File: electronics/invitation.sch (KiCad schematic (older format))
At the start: 40 parts, among them P1 USB Micro B, P10 Up Arrow, P11 Down Arrow, P2 Home btn, P3 Bottom Connections 1, P4 Left Arrow, P5 Right Arrow, P8 CONN_01X01, P9 CONN_01X02, U1 ATMEGA32U4-A, Y1 16 FA-238 Mhz

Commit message: Hero text fix + vr fix
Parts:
- P10: footprint newAssets:upArrow -> newAssets:upArrowSS
- P11: footprint newAssets:downArrow -> newAssets:downArrowSS
- P4: footprint newAssets:leftArrow -> newAssets:leftArrowSS
- P5: footprint newAssets:rightArrow -> newAssets:rightArrowSS
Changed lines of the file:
@@
 F 0 "P4" H 10050 2950 50  0000 C CNN
 F 1 "Left Arrow" H 10350 2850 50  0000 C CNN
-F 2 "newAssets:leftArrow" H 10050 2850 50  0001 C CNN
+F 2 "newAssets:leftArrowSS" H 10050 2850 50  0001 C CNN
 F 3 "" H 10050 2850 50  0000 C CNN
 	1    10050 2850
@@
 F 0 "P5" H 10100 3950 50  0000 C CNN
 F 1 "Right Arrow" H 10400 3850 50  0000 C CNN
-F 2 "newAssets:rightArrow" H 10100 3850 50  0001 C CNN
+F 2 "newAssets:rightArrowSS" H 10100 3850 50  0001 C CNN
 F 3 "" H 10100 3850 50  0000 C CNN
 	1    10100 3850
@@
 F 0 "P10" H 10000 5150 50  0000 C CNN
 F 1 "Up Arrow" H 10250 5050 50  0000 C CNN
-F 2 "newAssets:upArrow" H 10000 5050 50  0001 C CNN
+F 2 "newAssets:upArrowSS" H 10000 5050 50  0001 C CNN
 F 3 "" H 10000 5050 50  0000 C CNN
 	1    10000 5050
@@
 F 0 "P11" H 10100 6300 50  0000 C CNN
 F 1 "Down Arrow" H 10400 6200 50  0000 C CNN
-F 2 "newAssets:downArrow" H 10100 6200 50  0001 C CNN
+F 2 "newAssets:downArrowSS" H 10100 6200 50  0001 C CNN
 F 3 "" H 10100 6200 50  0000 C CNN
 	1    10100 6200

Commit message: pub in progress
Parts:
- P2: footprint newAssets:JMLogoFinal -> newAssets:JMLogoFinalSS
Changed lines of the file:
@@
 F 0 "P2" H 10100 1950 50  0000 C CNN
 F 1 "Home btn" H 10400 1850 50  0000 C CNN
-F 2 "newAssets:JMLogoFinal" H 10100 1850 50  0001 C CNN
+F 2 "newAssets:JMLogoFinalSS" H 10100 1850 50  0001 C CNN
 F 3 "" H 10100 1850 50  0000 C CNN
 	1    10100 1850

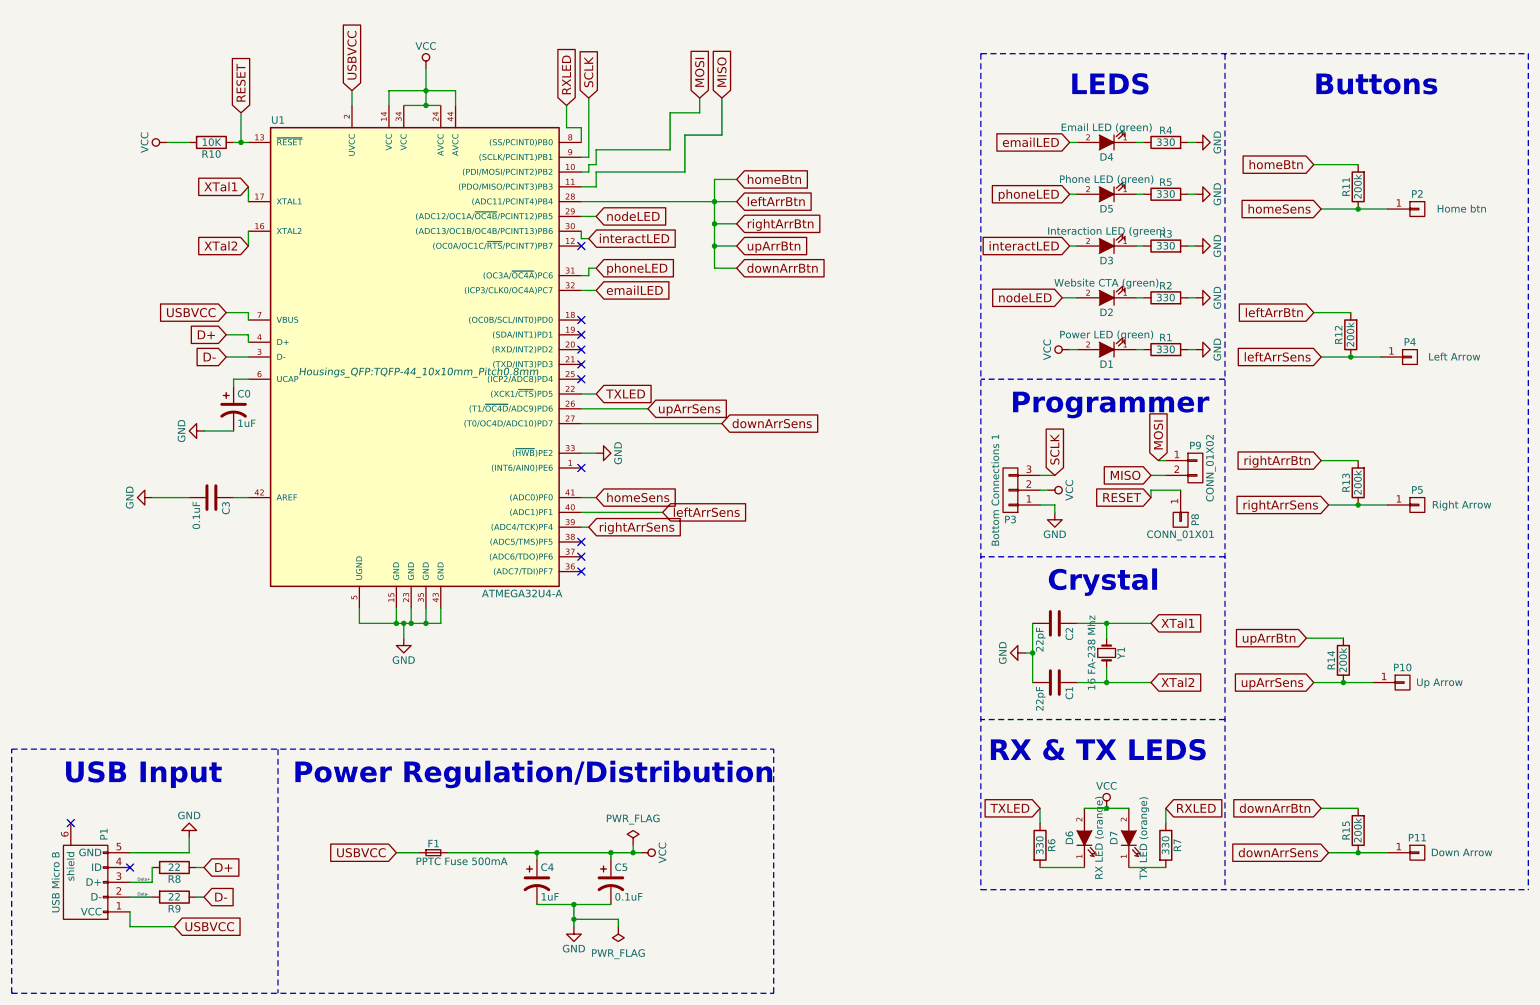
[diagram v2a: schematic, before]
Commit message: Business card finished.
To do:
- Implement keyboard functionality to website
- Test Arduino code + electronics
- Get electronics card purchased
- Implement instructions for VR page on desktop
- Final check of website copy prior to getting biz cards reprinted
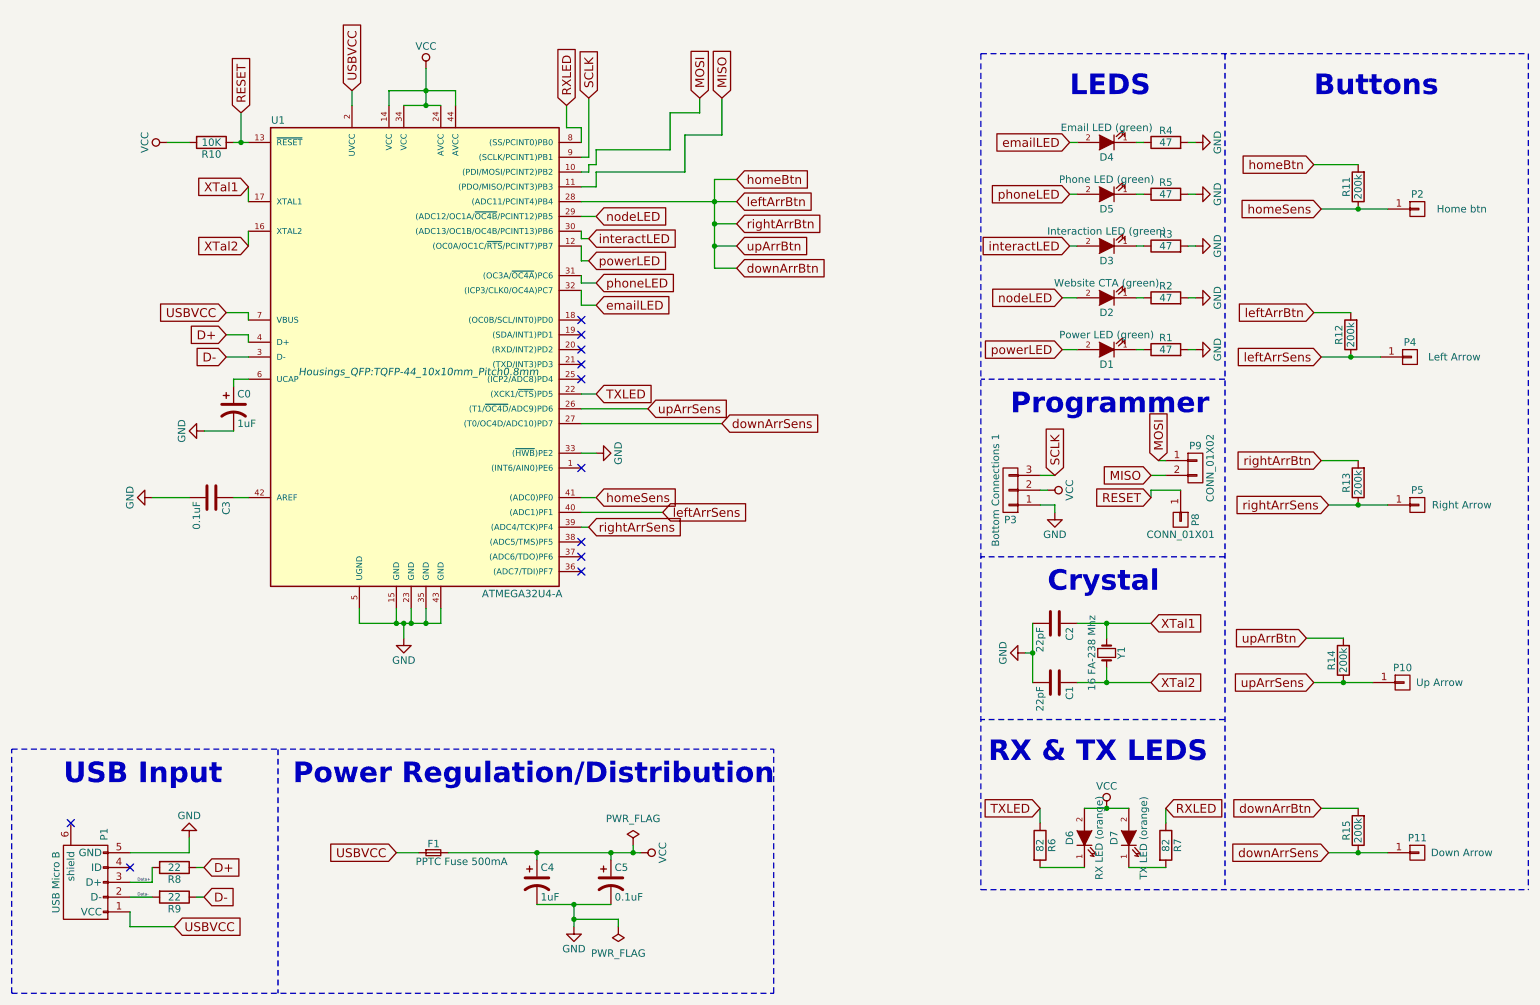
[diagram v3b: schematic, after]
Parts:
- R1, R2, R3, R4, R5: value 330 -> 47
- R6, R7: value 330 -> 82
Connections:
- net VCC: no longer D1.2 (A)
- net powerLED: now reaches U1.12 ((OC0A/OC1C/~RTS~/PCINT7)PB7)
- net powerLED: now also D1.2 (A)
- no-connect marks 12 -> 11
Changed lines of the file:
@@
 Sheet 1 1
 Title "Portfolio Business Card"
-Date "January 2017"
+Date "November 2018"
 Rev "1"
 Comp "James Miller"
@@
 P 7550 6150
 F 0 "R6" V 7630 6150 50  0000 C CNN
-F 1 "330" V 7550 6150 50  0000 C CNN
+F 1 "82" V 7550 6150 50  0000 C CNN
 F 2 "Resistors_SMD:R_0805" V 7480 6150 50  0001 C CNN
 F 3 "" H 7550 6150 50  0000 C CNN
@@
 P 8400 6150
 F 0 "R7" V 8480 6150 50  0000 C CNN
-F 1 "330" V 8400 6150 50  0000 C CNN
+F 1 "82" V 8400 6150 50  0000 C CNN
 F 2 "Resistors_SMD:R_0805" V 8330 6150 50  0001 C CNN
 F 3 "" H 8400 6150 50  0000 C CNN
@@
 	1    0    0    -1
 $EndComp
-NoConn ~ 4450 2100
 $Comp
 L power:GND #PWR06
@@
 $EndComp
 $Comp
-L power:VCC #PWR014
-U 1 1 5842A32B
-P 7750 2800
-F 0 "#PWR014" H 7750 2650 50  0001 C CNN
-F 1 "VCC" H 7750 2950 50  0000 C CNN
-F 2 "" H 7750 2800 50  0000 C CNN
-F 3 "" H 7750 2800 50  0000 C CNN
-	1    7750 2800
-	0    -1   -1   0
-$EndComp
-$Comp
 L Device:R R1
 U 1 1 5842A439
 P 8400 2800
 F 0 "R1" V 8480 2800 50  0000 C CNN
-F 1 "330" V 8400 2800 50  0000 C CNN
+F 1 "47" V 8400 2800 50  0000 C CNN
 F 2 "Resistors_SMD:R_0805" V 8330 2800 50  0001 C CNN
 F 3 "" H 8400 2800 50  0000 C CNN
@@
 P 8400 2450
 F 0 "R2" V 8480 2450 50  0000 C CNN
-F 1 "330" V 8400 2450 50  0000 C CNN
+F 1 "47" V 8400 2450 50  0000 C CNN
 F 2 "Resistors_SMD:R_0805" V 8330 2450 50  0001 C CNN
 F 3 "" H 8400 2450 50  0000 C CNN
@@
 P 8400 2100
 F 0 "R3" V 8480 2100 50  0000 C CNN
-F 1 "330" V 8400 2100 50  0000 C CNN
+F 1 "47" V 8400 2100 50  0000 C CNN
 F 2 "Resistors_SMD:R_0805" V 8330 2100 50  0001 C CNN
 F 3 "" H 8400 2100 50  0000 C CNN
@@
 P 8400 1400
 F 0 "R4" V 8480 1400 50  0000 C CNN
-F 1 "330" V 8400 1400 50  0000 C CNN
+F 1 "47" V 8400 1400 50  0000 C CNN
 F 2 "Resistors_SMD:R_0805" V 8330 1400 50  0001 C CNN
 F 3 "" H 8400 1400 50  0000 C CNN
@@
 P 8400 1750
 F 0 "R5" V 8480 1750 50  0000 C CNN
-F 1 "330" V 8400 1750 50  0000 C CNN
+F 1 "47" V 8400 1750 50  0000 C CNN
 F 2 "Resistors_SMD:R_0805" V 8330 1750 50  0001 C CNN
 F 3 "" H 8400 1750 50  0000 C CNN
@@
 Text GLabel 7750 1750 0    60   Input ~ 0
 phoneLED
-Text GLabel 4550 2250 2    60   Input ~ 0
+Text GLabel 4550 2350 2    60   Input ~ 0
 phoneLED
-Text GLabel 4550 2400 2    60   Input ~ 0
+Text GLabel 4550 2500 2    60   Input ~ 0
 emailLED
 Text GLabel 4350 1150 1    60   Input ~ 0
@@
 	7550 5900 7550 6000
 Wire Wire Line
-	4450 2400 4550 2400
-Wire Wire Line
-	4500 2250 4550 2250
-Wire Wire Line
-	4500 2300 4500 2250
-Wire Wire Line
-	4450 2300 4500 2300
-Wire Wire Line
 	7750 1750 7800 1750
 Wire Wire Line
@@
 Wire Wire Line
 	4550 1900 4450 1900
-Wire Wire Line
-	7750 2800 7800 2800
 Wire Wire Line
 	8550 2800 8600 2800
@@
 Wire Notes Line
 	10850 800  10850 6450
+Text GLabel 7700 2800 0    60   Input ~ 0
+powerLED
+Wire Wire Line
+	7700 2800 7800 2800
+Text GLabel 4500 2200 2    60   Input ~ 0
+powerLED
+Wire Wire Line
+	4450 2100 4450 2200
+Wire Wire Line
+	4450 2200 4500 2200
+Wire Wire Line
+	4450 2300 4450 2350
+Wire Wire Line
+	4450 2350 4550 2350
+Wire Wire Line
+	4450 2400 4450 2500
+Wire Wire Line
+	4450 2500 4550 2500
 $EndSCHEMATC

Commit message: Completed WebVR animation of icon on scroll, V8 of PCB is in fabrication
To do:
- Implement webvr-polyfill for mobile
- More intuitive UX for webvr laptop experience
- Fix getOSVersion.js HOC (in Lincoln)
- Auto go-to webvr page on mobile if on iOS or android version .4 or higher
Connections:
- net downArrBtn: now also U1.25 ((ICP2/ADC8)PD4); no longer R11.2, R12.2, R13.2, R14.2, U1.28 ((ADC11/PCINT4)PB4)
- net rightArrBtn: now reaches U1.1 ((INT6/AIN0)PE6)
- net rightArrBtn: now also R13.2, R14.2
- new net homeBtn: R11.2, R12.2, U1.28 ((ADC11/PCINT4)PB4)
- no-connect marks 11 -> 9
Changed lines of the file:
@@
 Title "Portfolio Business Card"
 Date "November 2018"
-Rev "1"
+Rev "8"
 Comp "James Miller"
 Comment1 ""
@@
 $EndComp
 $Comp
-L invitation-rescue:ATMEGA32U4-A U1
-U 1 1 5840CFD0
-P 3350 2950
-F 0 "U1" H 2400 4650 50  0000 C CNN
-F 1 "ATMEGA32U4-A" H 4050 1450 50  0000 C CNN
-F 2 "Housings_QFP:TQFP-44_10x10mm_Pitch0.8mm" H 3350 2950 50  0000 C CIN
-F 3 "" H 4450 4050 50  0000 C CNN
-	1    3350 2950
-	1    0    0    -1
-$EndComp
-$Comp
 L Device:Crystal_Small Y1
 U 1 1 58744F16
@@
 Text Label 1450 6500 0    20   ~ 0
 Data-
-NoConn ~ 4450 3600
 $Comp
 L invitation-rescue:LED D6
@@
 Text GLabel 5500 1800 2    60   Input ~ 0
 leftArrBtn
-Text GLabel 5500 1950 2    60   Input ~ 0
+Text GLabel 4900 3500 2    60   Input ~ 0
 rightArrBtn
-Text GLabel 5500 2100 2    60   Input ~ 0
+Text GLabel 5450 3600 2    60   Input ~ 0
 upArrBtn
-Text GLabel 5500 2250 2    60   Input ~ 0
+Text GLabel 4900 3000 2    60   Input ~ 0
 downArrBtn
 Wire Wire Line
@@
 	5350 1800 5500 1800
 Connection ~ 5350 1800
-Wire Wire Line
-	5350 1950 5500 1950
-Wire Wire Line
-	5350 2100 5500 2100
-Wire Wire Line
-	5350 1800 5350 1950
-Connection ~ 5350 1950
-Wire Wire Line
-	5350 1950 5350 2100
-Wire Wire Line
-	5500 2250 5350 2250
-Wire Wire Line
-	5350 2250 5350 2100
-Connection ~ 5350 2100
 Wire Wire Line
 	9700 1850 9900 1850
@@
 NoConn ~ 4450 4200
 NoConn ~ 4450 4100
-NoConn ~ 4450 3000
 NoConn ~ 4450 2900
 NoConn ~ 4450 2800
@@
 Wire Wire Line
 	4450 2500 4550 2500
+$Comp
+L invitation-rescue:ATMEGA32U4-A U1
+U 1 1 5840CFD0
+P 3350 2950
+F 0 "U1" H 2400 4650 50  0000 C CNN
+F 1 "ATMEGA32U4-A" H 4050 1450 50  0000 C CNN
+F 2 "Housings_QFP:TQFP-44_10x10mm_Pitch0.8mm" H 3350 2950 50  0000 C CIN
+F 3 "" H 4450 4050 50  0000 C CNN
+	1    3350 2950
+	1    0    0    -1
+$EndComp
+Wire Wire Line
+	4450 3600 4800 3600
+Wire Wire Line
+	4800 3600 4800 3500
+Wire Wire Line
+	4800 3500 4900 3500
+Wire Wire Line
+	4800 3600 5450 3600
+Connection ~ 4800 3600
+Wire Wire Line
+	4900 3000 4450 3000
 $EndSCHEMATC

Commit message: Updated npm modules + code splitting functionality, found that the youtube chrome iOS bug is for all websites (hopefully this will be fixed by them soon), electronic card v13 submitted - To complete 1. Test that appropriate content appears on all devices - fix gyroscope movement on mobile devices 2. Create content for instruction page on headset webvr + mobile webvr + mobile + laptop 3. Test electronic card
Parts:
- P1: footprint Connect:USB_Micro-B -> 10103594-0001LF:FCI_10103594-0001LF; symbol invitation-rescue:USB_OTG -> invitation-rescue:USB_OTG-invitation-rescue
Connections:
- no-connect marks 9 -> 8
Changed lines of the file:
@@
 Sheet 1 1
 Title "Portfolio Business Card"
-Date "November 2018"
-Rev "8"
+Date "April 2019"
+Rev "11"
 Comp "James Miller"
 Comment1 ""
@@
 $EndComp
 $Comp
-L invitation-rescue:USB_OTG P1
+L invitation-rescue:USB_OTG-invitation-rescue P1
 U 1 1 5840E12E
 P 1100 6400
 F 0 "P1" H 1425 6275 50  0000 C CNN
 F 1 "USB Micro B" H 1100 6600 50  0000 C CNN
-F 2 "Connect:USB_Micro-B" V 1050 6300 50  0001 C CNN
+F 2 "10103594-0001LF:FCI_10103594-0001LF" V 1050 6300 50  0001 C CNN
 F 3 "" V 1050 6300 50  0000 C CNN
 	1    1100 6400
 	0    -1   -1   0
 $EndComp
-NoConn ~ 1000 6000
 NoConn ~ 1400 6300
 Text GLabel 1700 6700 2    60   Input ~ 0
